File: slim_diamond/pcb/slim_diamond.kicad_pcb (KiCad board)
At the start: 2 copper layers, 87.6 x 92.3 mm, 34 parts, among them J1 JST PH 2.0 battery, SW1 pinky, SW10 index_bottom, SW11 thumb_outer, SW12 thumb_inner, SW13 MSK-12C02, SW14 TS-1187A reset, SW2 ring_top, SW3 ring_home, SW4 ring_bottom, SW5 middle_top, SW6 middle_home, SW7 middle_bottom, SW8 index_top, SW9 index_home, U1 XIAO nRF52840 / Super52840

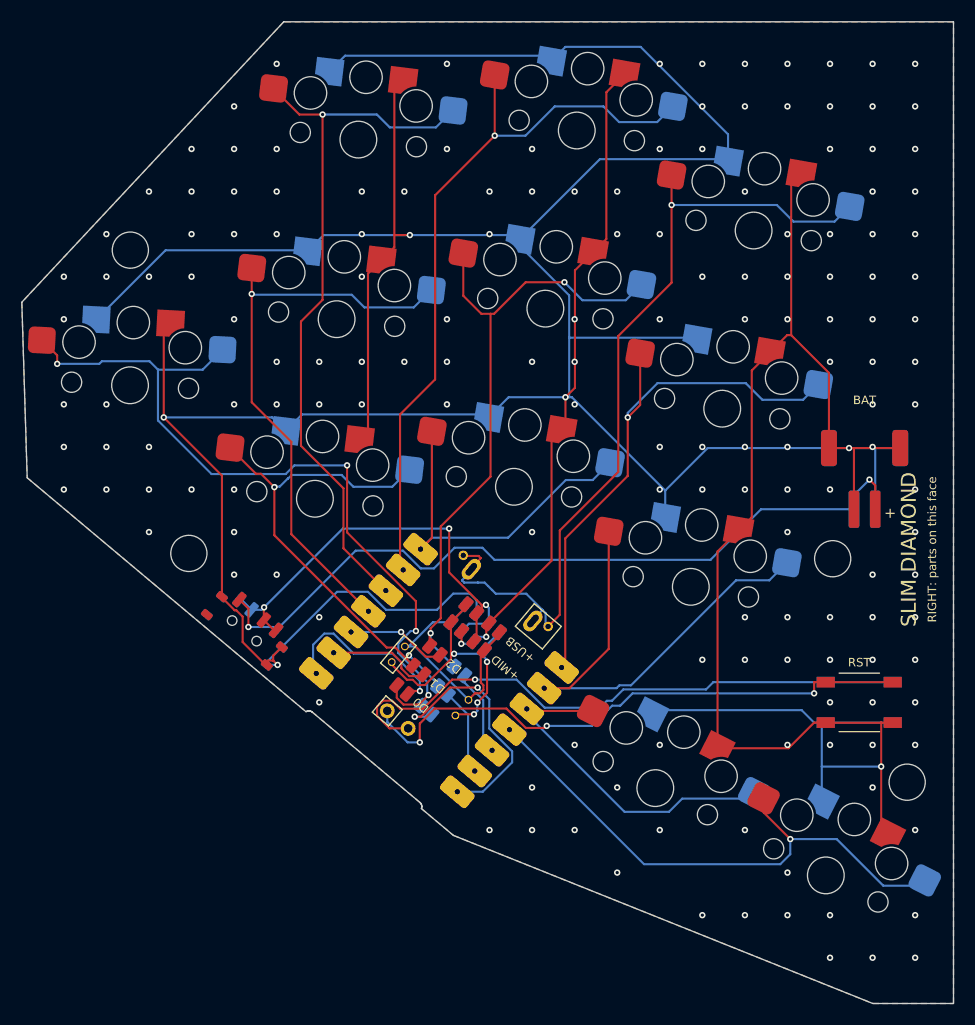
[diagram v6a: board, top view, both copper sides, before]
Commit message: Enlarge the battery and P0.09 fill holes as far as the pads allow
The holes fed with solder to reach the module's battery pads and the
Super52840's P0.09 pad were 0.5 mm. Solder might not flow through them.
- Battery (BATM, BATU): 0.6 mm drill, 0.88 mm ring (0.14 annular;
  JLCPCB's minimum is 0.13). 0.7 left too thin a ring. The drill stays
  inside both modules' pads, and the mirror copy stays 0.17 mm clear of
  the Super52840's GPIO row under the other half's module, at the
  photos' nearest reading.
- P0.09 at the Super52840's pad: 0.6 mm drill, 1.0 mm ring, inside
  the pad at all three readings of its position.

A taller oval ring closed the one track channel to L1/L13 past the
USB-C leg holes, so the battery rings stay round. The fence round the
leg holes is now 0.25 mm (KiCad's hole clearance), down from 0.4.

Routed at 0.14 mm. Severity-all DRC: clean, 0 unconnected. The pin map
is unchanged. The contact check passes for both modules in both mounts
at all three GPIO row readings. BUILD.md gives the new hole size and
how to fill it.

Co-Authored-By: Claude Opus 5.5 <noreply@anthropic.com>
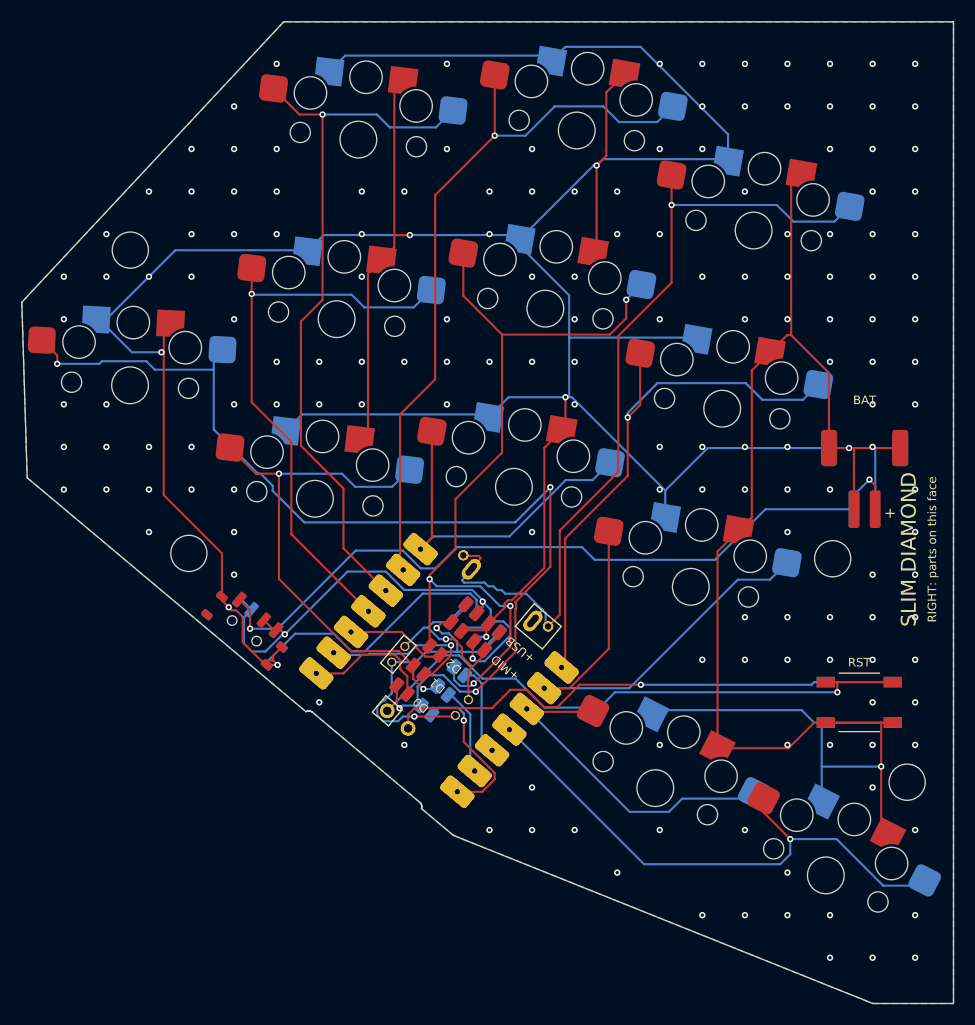
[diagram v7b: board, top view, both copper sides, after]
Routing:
- net K_pinky: track 77.0 -> 97.8 mm
- net GND: track 536.3 -> 518.3 mm, vias 169 -> 170
- net K_middle_home: track 61.6 -> 78.1 mm, vias 2 -> 4
- net X_L14: track 23.4 -> 14.9 mm, vias 2 -> 1
- net RST_R: track 56.5 -> 49.5 mm
- net VBAT: track 43.3 -> 50.3 mm
- net X_L2: track 9.78 -> 15.7 mm, vias 0 -> 1
- net X_L1: track 17.4 -> 12.3 mm, vias 1 -> 0
- net BATU: track 27.1 -> 32.1 mm, vias 4 -> 2
- net BATM: track 23.6 -> 21.3 mm, vias 0 -> 1
- net K_ring_bottom: track 47.2 -> 49.1 mm
- net RST_L: track 54.8 -> 54.3 mm, vias 3 -> 1
- net X_L3: track 9.42 -> 9.47 mm, vias 1 -> 0

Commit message: Hold the Slim Diamond board to JLCPCB's limits, and add pre-order checks
The board is made in a single batch, so every check that can run before
ordering now does.

JLCPCB's 2-layer limits, encoded in pcb/slim_diamond.kicad_dru so the
DRC enforces them, found two things:
- The battery fill holes' ring was 0.14 mm; JLCPCB needs 0.18. They
  are now 0.6 mm drills in 0.96 mm rings, 0.02 mm further in. The mirror
  copy still clears the Super52840's GPIO row (0.15 mm at the nearest
  photo reading, 0.29 at the middle one), and the drill stays inside both
  modules' pads.
- Silkscreen: text is now 1.0 mm high with 0.15 strokes, and lines are
  0.15 (they were 0.8 and 0.12).

Tracks and vias are kept out of a strip under the module's chip antenna,
on both mounts (the selector and P0.09 wiring ran under it). Routed at
0.15 mm tracks and 0.14 clearance. Severity-all DRC under JLCPCB's rules:
clean, 0 unconnected. The pin map is unchanged.

check_pcb.py audits every net against its intent: each key, the D0-D2
jumpers, the battery path and selector rows, reset, no lone pads, no
tracks under the antenna. It also checks the firmware's pin lists for
both halves. ALL CLEAR. The fab files are checked too: drill counts per
tool match the design, slots meet JLCPCB's minimums, and the outline is
87.55 x 92.25 mm.

fab.sh also writes 1:1 PDFs of both faces to lay the real parts on.
The README gets a "Before ordering" checklist, and BUILD.md a
pre-tinning step for the module's underside pads.

Co-Authored-By: Claude Opus 5.5 <noreply@anthropic.com>
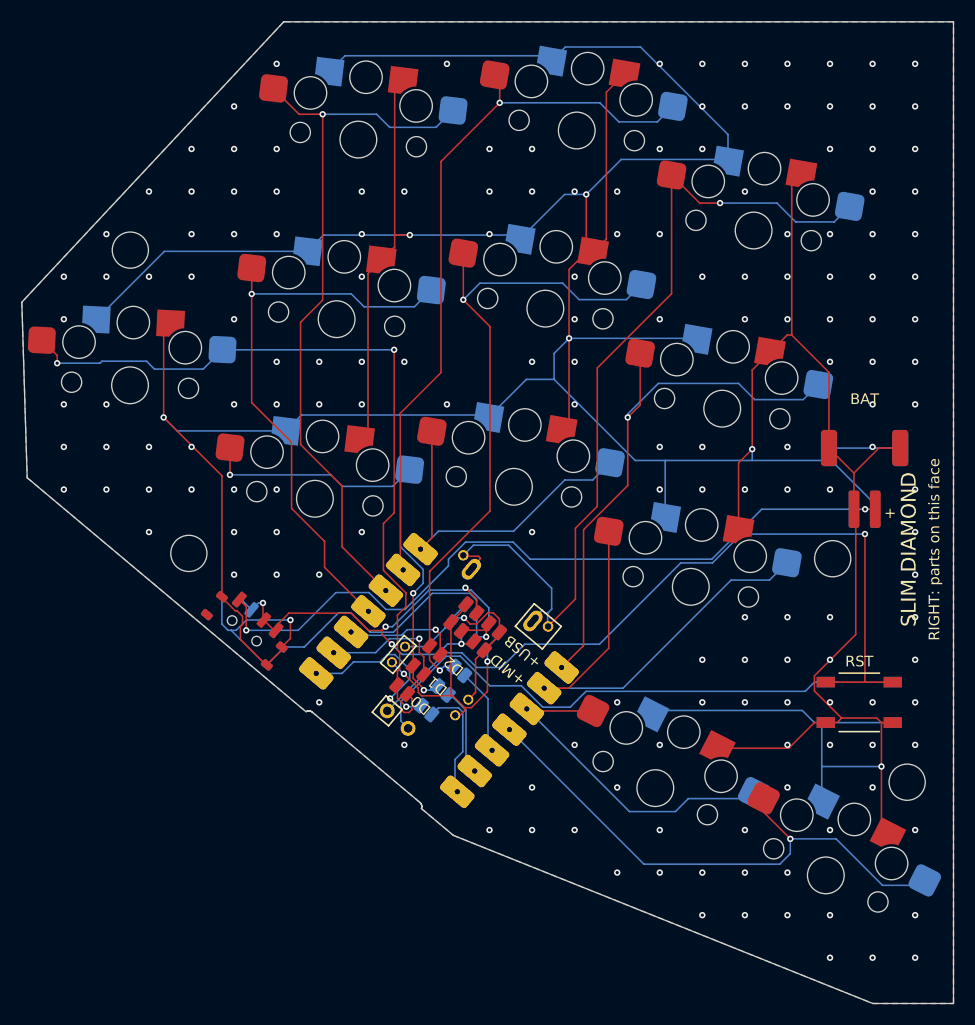
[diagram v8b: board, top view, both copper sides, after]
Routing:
- net K_pinky: track 97.8 -> 72.8 mm, vias 4 -> 3
- net RST_L: track 54.3 -> 73.1 mm
- net K_middle_home: track 78.1 -> 63.1 mm, vias 4 -> 2
- net GND: track 518.3 -> 531.9 mm, vias 170 -> 177
- net X_L1: track 12.3 -> 17.9 mm, vias 0 -> 1
- net K_ring_bottom: track 49.1 -> 43.6 mm, vias 2 -> 3
- net VBAT: track 50.3 -> 45.9 mm, vias 3 -> 5
- net RST_R: track 49.5 -> 53.8 mm, vias 1 -> 0
- net K_index_top: track 81.6 -> 85.6 mm
- net BATU: track 32.1 -> 28.4 mm
- net X_L14: track 14.9 -> 11.2 mm, vias 1 -> 0
- net X_L2: track 15.7 -> 12.1 mm
- net BAT+: track 73.5 -> 70.0 mm
- net BATM: track 21.3 -> 22.7 mm
- net X_L3: track 9.47 -> 10.8 mm, vias 0 -> 1
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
